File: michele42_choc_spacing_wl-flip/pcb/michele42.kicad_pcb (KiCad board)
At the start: 2 copper layers, 139.6 x 89.8 mm, 93 parts, among them J1 Battery, J2 OLED-5Pin, J4 LED, SW1 SW_Power, U1 MCU_Nice_Nano_V2

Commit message: Small fixes and images
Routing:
- added copper zone on B.Cu, net (none)
- added copper zone on F.Cu, net (none)
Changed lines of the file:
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@@
   (segment (start 170.789458 118.990542) (end 170.749458 118.990542) (width 0.25) (layer "B.Cu") (net 73))
   (segment (start 201.71 108.97) (end 201.71 111.74) (width 0.25) (layer "B.Cu") (net 73))
+  (zone (net 0) (net_name "") (layers "F&B.Cu") (hatch edge 0.5)
+    (connect_pads (clearance 0.5))
+    (min_thickness 0.25) (filled_areas_thickness no)
+    (fill yes (thermal_gap 0.5) (thermal_bridge_width 0.5) (island_removal_mode 1) (island_area_min 10))
+    (polygon
+      (pts
+        (xy 64.19 53.85)
+        (xy 211.15 54.75)
+        (xy 209.75 148.63)
+        (xy 64.09 148.83)
+      )
+    )
+  )
 )

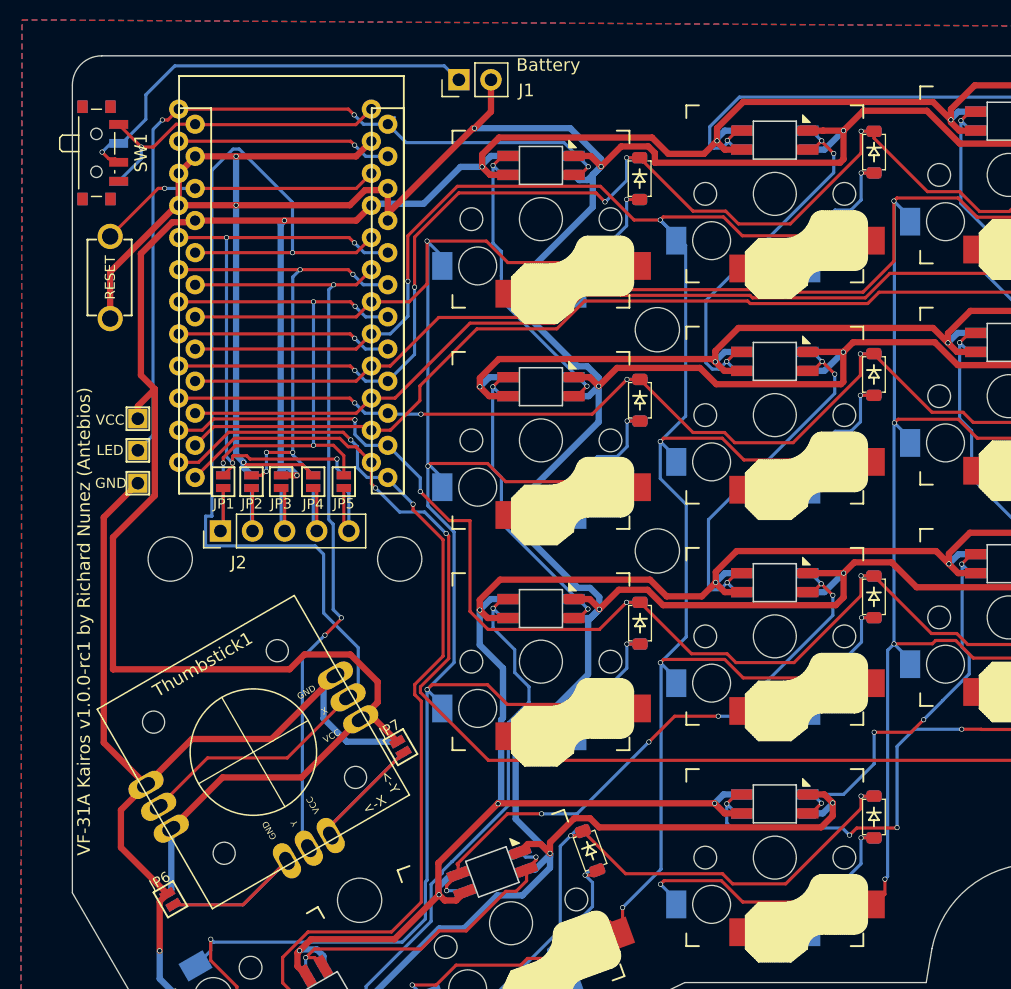
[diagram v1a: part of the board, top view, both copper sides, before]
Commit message: Relocate mounting holes to make room for battery
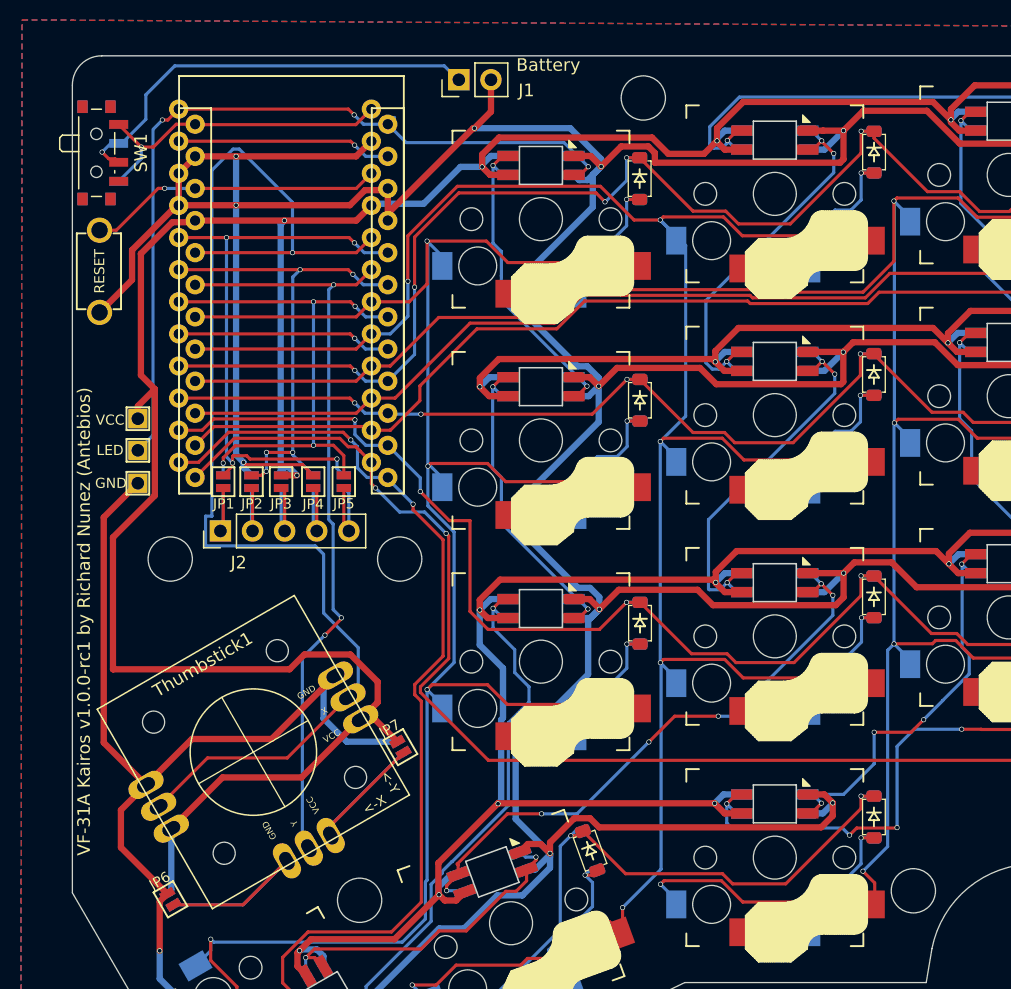
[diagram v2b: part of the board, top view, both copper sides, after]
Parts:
- moved H2 33.7 mm to (134.7, 122.7)
- moved H1 18.4 mm to (113.3, 60.0)
- moved RSW1 0.97 mm to (70.3, 73.7)
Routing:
- net Column 1: track 193.9 -> 192.2 mm
- net VCC: track 682.8 -> 681.9 mm
- net Column 2: track 205.5 -> 206.3 mm
- net RESET: track 22.8 -> 23.4 mm
